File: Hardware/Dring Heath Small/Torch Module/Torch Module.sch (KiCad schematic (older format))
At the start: 79 parts, among them J1 Torch, J10 Module conn, J11 Conn_01x18_Male, J12 Conn_01x02_Male, J14 Conn_01x02_Male, J15 Module conn, J2 Module3, J3 Conn_01x18_Male, J4 Limit, J6 8P8C_LED_Shielded, J7 Module1, J8 Torch, J9 2.54 pin, K1 G6E, Q1 IRLML2402, Q2 IRLML2402, Q3 IRLML2402, Q4 IRLML2402, Q5 IRLML2402, U1 ULN2002, U2 NCV8114ASN150T1G, U3 ADS1115IDGS

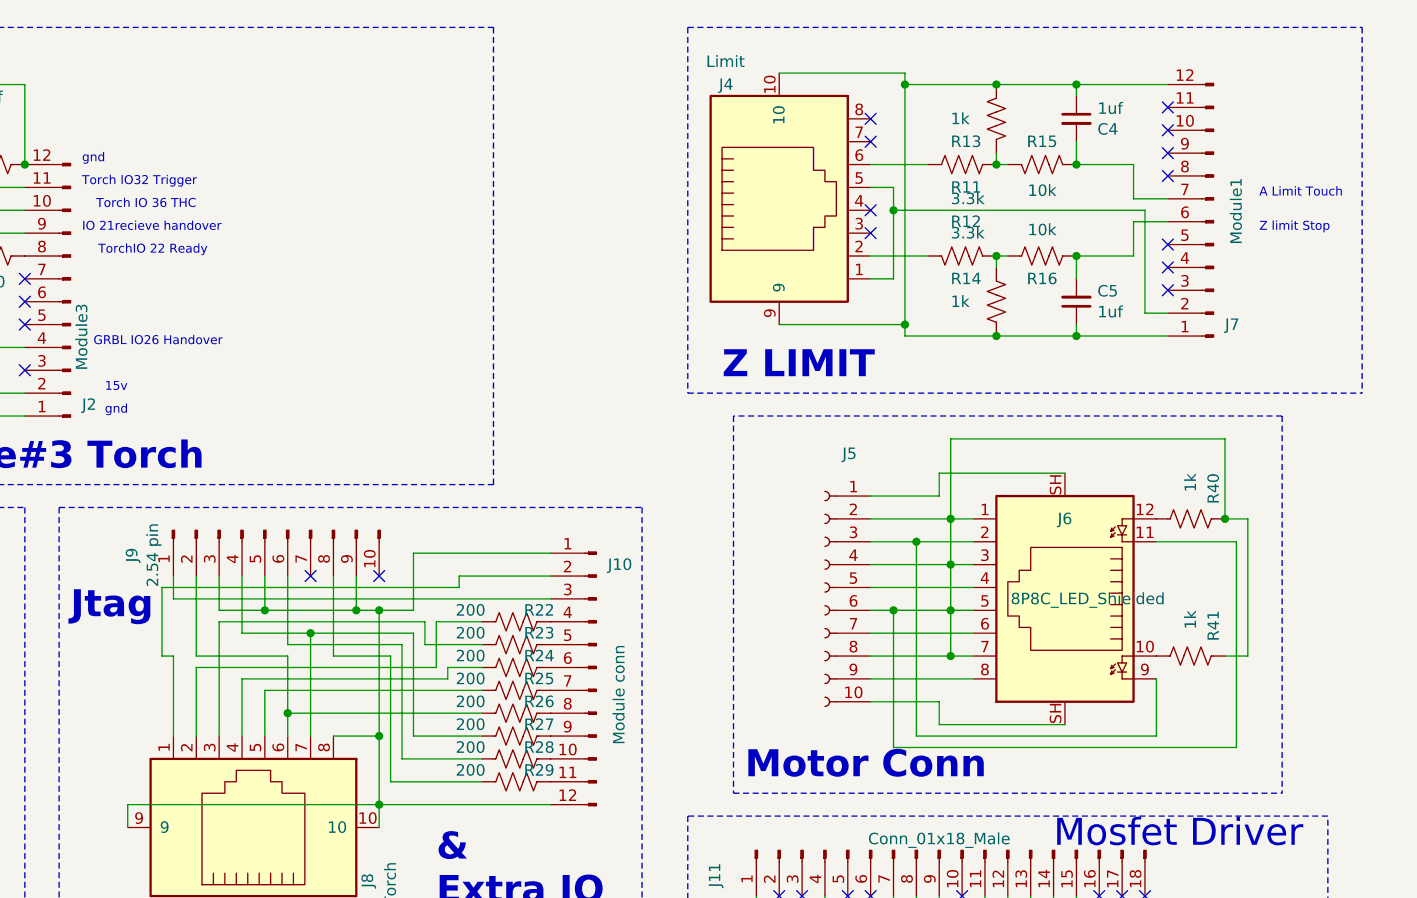
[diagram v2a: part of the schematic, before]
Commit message: Updated torch module boards for external reset
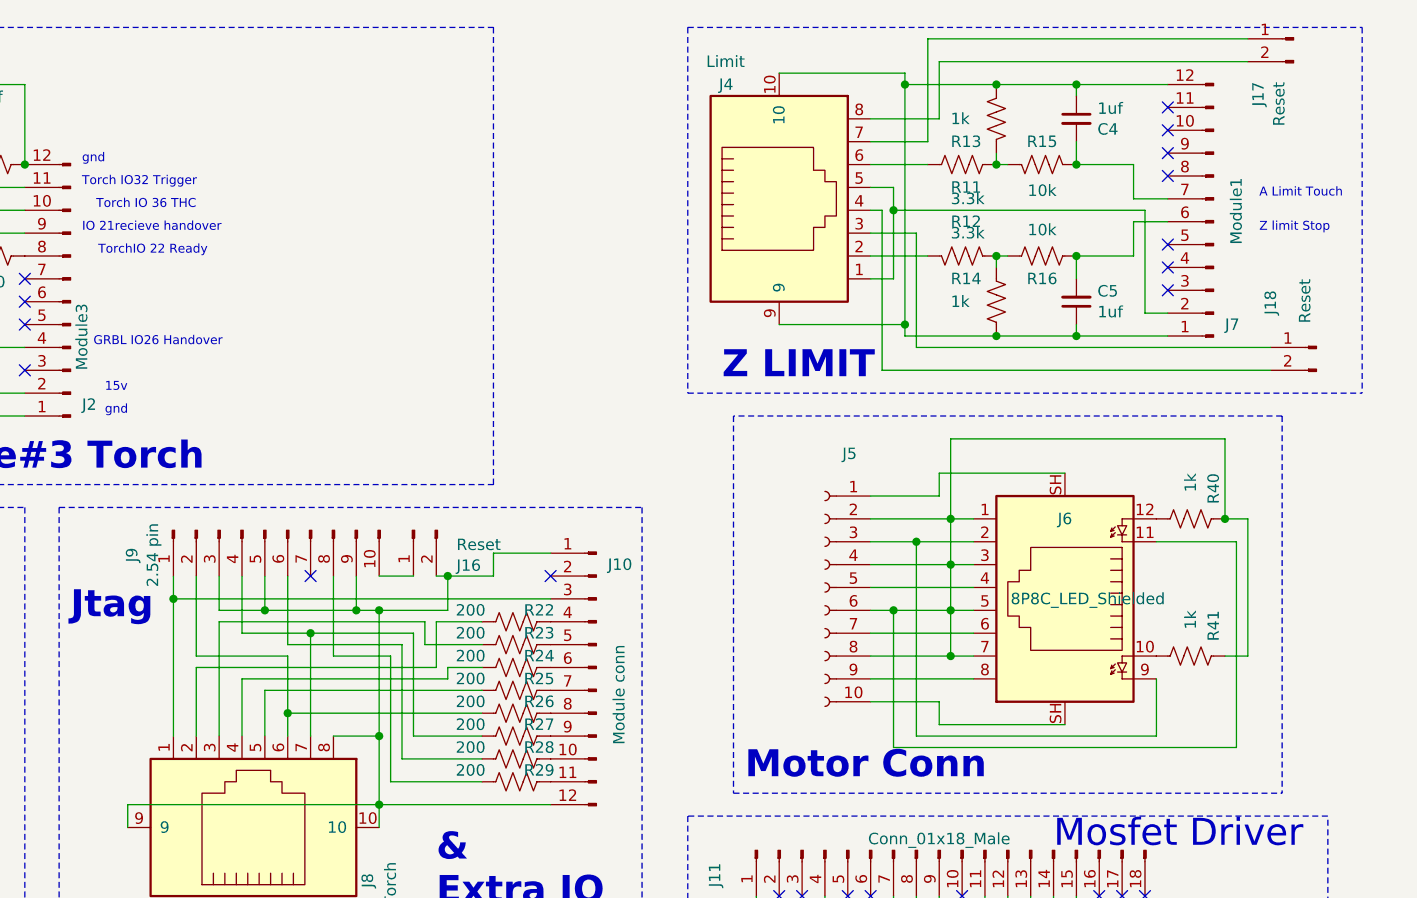
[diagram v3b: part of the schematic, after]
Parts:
- added J16, J17, J18: Reset, Connector_PinHeader_2.54mm:PinHeader_1x02_P2.54mm_Vertical, symbol Connector:Conn_01x02_Male
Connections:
- net at J4.3: now also J18.1 (Pin_1)
- net at J4.4: now also J18.2 (Pin_2)
- net at J4.7: now also J17.1 (Pin_1)
- net at J4.8: now also J17.2 (Pin_2)
- net at J10.1 (Pin_1), J10.12 (Pin_12), J8.10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: now also J16.2 (Pin_2)
- net at J10.2 (Pin_2): no longer J8.1
- net at J10.3 (Pin_3), J9.1 (Pin_1): now also J8.1
- net at J9.10 (Pin_10): now also J16.1 (Pin_1)
- no-connect marks 46 -> 42
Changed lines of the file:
@@
 Connection ~ 9100 1000
 Connection ~ 9100 2100
-NoConn ~ 8550 1150
-NoConn ~ 8550 1250
-NoConn ~ 8550 1550
-NoConn ~ 8550 1650
 NoConn ~ 9850 1900
 NoConn ~ 9850 1800
@@
 Wire Wire Line
 	2400 2550 2800 2550
-$Comp
-L Connector:Conn_01x10_Male J9
-U 1 1 600FA13A
-P 5900 2950
-F 0 "J9" H 6008 3531 50  0000 C CNN
-F 1 "2.54 pin" H 6008 3440 50  0000 C CNN
-F 2 "Connector_PinHeader_2.54mm:PinHeader_2x05_P2.54mm_Vertical" H 5900 2950 50  0001 C CNN
-F 3 "~" H 5900 2950 50  0001 C CNN
-	1    5900 2950
-	0    -1   1    0
-$EndComp
 Text Notes 5050 3350 0    118  ~ 24
 Jtag
@@
 	6600 3350 6600 3450
 Wire Wire Line
-	6550 3300 6550 3050
-Wire Wire Line
 	5800 3150 5800 3400
 Wire Wire Line
@@
 Wire Wire Line
 	6400 4250 6400 4150
-Wire Wire Line
-	6750 3200 5450 3200
-Wire Wire Line
-	5450 3200 5450 3500
-Wire Wire Line
-	5450 3500 5500 3500
-Wire Wire Line
-	5500 3500 5500 3850
 Wire Notes Line
 	5000 2850 5000 4650
@@
 $EndComp
 Wire Wire Line
-	6750 3200 6750 3150
-Wire Wire Line
-	6750 3150 7150 3150
-Wire Wire Line
 	6650 3350 6650 3550
 Wire Wire Line
@@
 Wire Wire Line
 	6100 3400 6550 3400
-NoConn ~ 6400 3150
 NoConn ~ 6100 3150
 Wire Wire Line
@@
 	6400 4150 7150 4150
 Wire Wire Line
-	6550 3050 7150 3050
-Wire Wire Line
 	6400 3850 6400 3300
 Connection ~ 6400 3850
 Connection ~ 6400 3300
-Wire Wire Line
-	6400 3300 6550 3300
 Wire Wire Line
 	6000 3500 6000 3750
@@
 Wire Wire Line
 	8650 3300 8900 3300
+$Comp
+L Connector:Conn_01x02_Male J16
+U 1 1 6029708A
+P 6550 2950
+F 0 "J16" V 6704 2762 50  0000 R CNN
+F 1 "Reset" V 6613 2762 50  0000 R CNN
+F 2 "Connector_PinHeader_2.54mm:PinHeader_1x02_P2.54mm_Vertical" H 6550 2950 50  0001 C CNN
+F 3 "~" H 6550 2950 50  0001 C CNN
+	1    6550 2950
+	0    -1   1    0
+$EndComp
+$Comp
+L Connector:Conn_01x10_Male J9
+U 1 1 600FA13A
+P 5900 2950
+F 0 "J9" H 6008 3531 50  0000 C CNN
+F 1 "2.54 pin" H 6008 3440 50  0000 C CNN
+F 2 "Connector_PinHeader_2.54mm:PinHeader_2x05_P2.54mm_Vertical" H 5900 2950 50  0001 C CNN
+F 3 "~" H 5900 2950 50  0001 C CNN
+	1    5900 2950
+	0    -1   1    0
+$EndComp
+Wire Wire Line
+	6400 3150 6550 3150
+$Comp
+L Connector:Conn_01x02_Male J17
+U 1 1 6038F2D5
+P 10400 800
+F 0 "J17" V 10554 612 50  0000 R CNN
+F 1 "Reset" V 10463 612 50  0000 R CNN
+F 2 "Connector_PinHeader_2.54mm:PinHeader_1x02_P2.54mm_Vertical" H 10400 800 50  0001 C CNN
+F 3 "~" H 10400 800 50  0001 C CNN
+	1    10400 800
+	-1   0    0    -1
+$EndComp
+$Comp
+L Connector:Conn_01x02_Male J18
+U 1 1 60391CC7
+P 10500 2150
+F 0 "J18" V 10700 2400 50  0000 R CNN
+F 1 "Reset" V 10550 2450 50  0000 R CNN
+F 2 "Connector_PinHeader_2.54mm:PinHeader_1x02_P2.54mm_Vertical" H 10500 2150 50  0001 C CNN
+F 3 "~" H 10500 2150 50  0001 C CNN
+	1    10500 2150
+	-1   0    0    -1
+$EndComp
+Wire Wire Line
+	8550 1250 8800 1250
+Wire Wire Line
+	8800 1250 8800 800
+Wire Wire Line
+	8800 800  10200 800
+Wire Wire Line
+	8550 1150 8850 1150
+Wire Wire Line
+	8850 1150 8850 900
+Wire Wire Line
+	8850 900  10200 900
+Wire Wire Line
+	8550 1650 8750 1650
+Wire Wire Line
+	8750 1650 8750 2150
+Wire Wire Line
+	8750 2150 10300 2150
+Wire Wire Line
+	8550 1550 8600 1550
+Wire Wire Line
+	8600 1550 8600 2250
+Wire Wire Line
+	8600 2250 10300 2250
+Wire Wire Line
+	6700 3300 6700 3150
+Wire Wire Line
+	6700 3150 6900 3150
+Wire Wire Line
+	6900 3150 6900 3050
+Wire Wire Line
+	6900 3050 7150 3050
+Wire Wire Line
+	6400 3300 6700 3300
+Wire Wire Line
+	6650 3150 6700 3150
+Connection ~ 6700 3150
+Wire Wire Line
+	5500 3250 5500 3850
+Connection ~ 5500 3250
+NoConn ~ 7150 3150
 $EndSCHEMATC
